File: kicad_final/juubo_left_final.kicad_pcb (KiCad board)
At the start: 2 copper layers, 145.5 x 125.5 mm, 50 parts

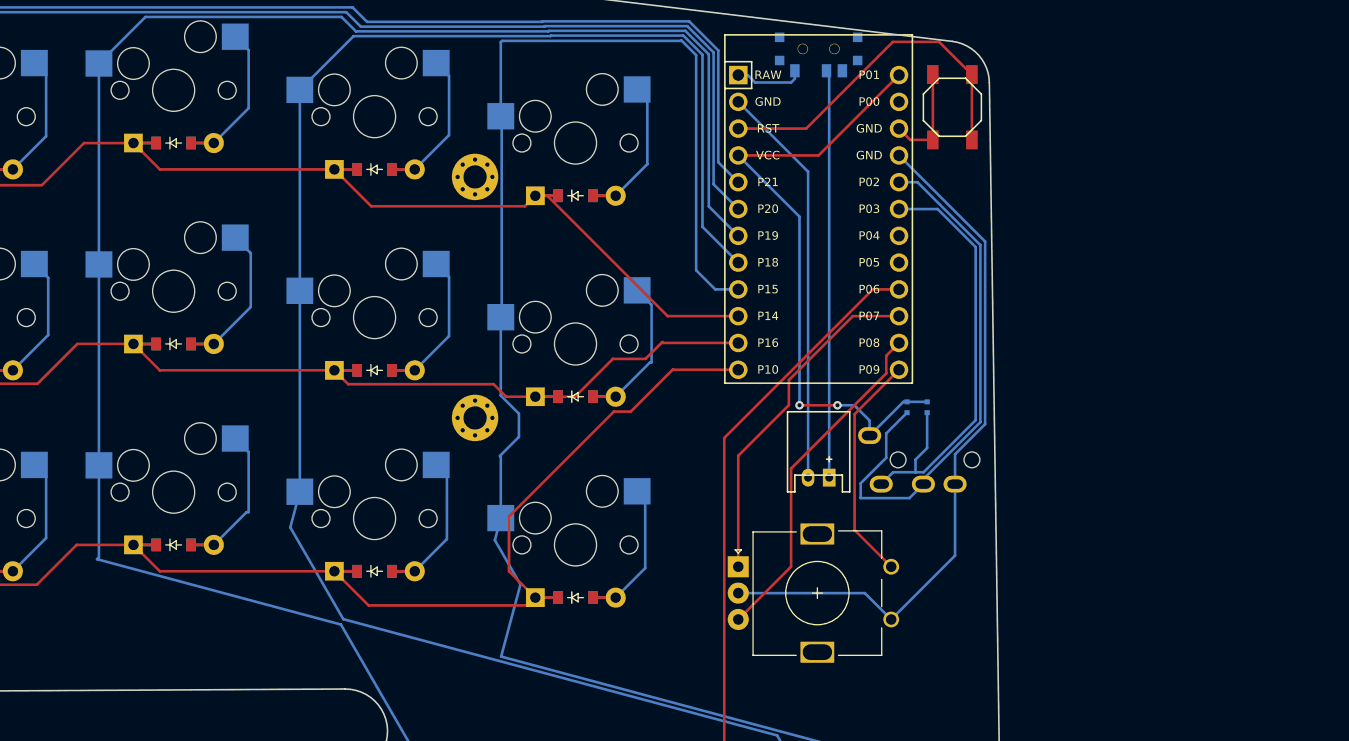
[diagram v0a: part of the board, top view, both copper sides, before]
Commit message: Add qmk, gerber, kicad files
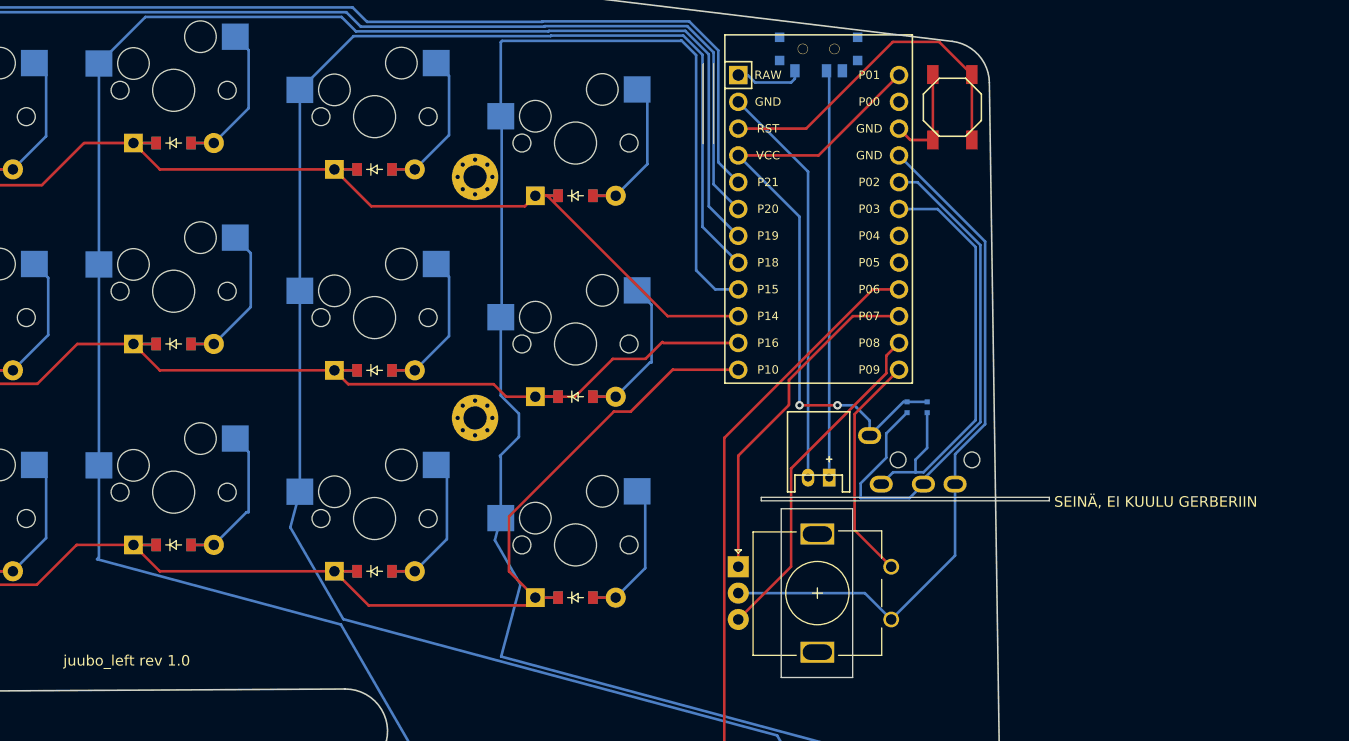
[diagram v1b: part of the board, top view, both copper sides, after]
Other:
- outline, holes or cut-outs redrawn
- board text added: "ROTARY NUPPI 16MM"
- board text added: "SEINÄ, EI KUULU GERBERIIN"
- board text added: "juubo_left rev 1.0"
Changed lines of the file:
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@@
       (outputformat 1)
       (mirror false)
-      (drillshape 1)
+      (drillshape 0)
       (scaleselection 1)
-      (outputdirectory "")
+      (outputdirectory "../gerbers/juube_lefti_final")
     )
   )
@@
       (net 36 "P2") (solder_mask_margin 0.102))
   )
+  (gr_line (start 177.67 57.4) (end 177.67 49.8)
+    (stroke (width 0.05) (type default)) (layer "Edge.Cuts"))
   (gr_arc (start 142.722221 109.098913) (mid 145.877217 110.612025) (end 146.634761 114.028112)
     (stroke (width 0.15) (type solid)) (layer "Edge.Cuts"))
+  (gr_rect (start 182.175 90.925) (end 209.485 91.255)
+    (stroke (width 0.05) (type default)) (fill none) (layer "Edge.Cuts"))
   (gr_arc (start 95.717823 43.355782) (mid 95.889609 43.314727) (end 96.063039 43.281294)
     (stroke (width 0.15) (type solid)) (layer "Edge.Cuts"))
@@
   (gr_arc (start 200.280578 47.697143) (mid 202.774498 48.99265) (end 203.800645 51.608921)
     (stroke (width 0.15) (type solid)) (layer "Edge.Cuts"))
+  (gr_line (start 176.67 57.4) (end 176.67 49.8)
+    (stroke (width 0.05) (type default)) (layer "Edge.Cuts"))
   (gr_line (start 202.748997 162.877717) (end 221.659673 144.499586)
     (stroke (width 0.15) (type default)) (layer "Edge.Cuts"))
@@
   (gr_line (start 143.900962 125.473809) (end 146.634761 114.028112)
     (stroke (width 0.15) (type solid)) (layer "Edge.Cuts"))
+  (gr_rect (start 184.065 92.006) (end 190.84 108.006)
+    (stroke (width 0.05) (type default)) (fill none) (layer "Edge.Cuts"))
   (gr_arc (start 202.748997 162.877717) (mid 200.311135 164.046527) (end 197.688861 163.388522)
     (stroke (width 0.15) (type default)) (layer "Edge.Cuts"))
   (gr_arc (start 221.356714 139.908256) (mid 222.292209 142.152188) (end 221.659673 144.499586)
     (stroke (width 0.15) (type default)) (layer "Edge.Cuts"))
+  (gr_text "juubo_left rev 1.0" (at 116 107) (layer "F.SilkS")
+    (effects (font (size 1 1) (thickness 0.1)) (justify left bottom))
+  )
+  (gr_text "SEINÄ, EI KUULU GERBERIIN" (at 209.94 91.94) (layer "F.SilkS")
+    (effects (font (size 1 1) (thickness 0.15)) (justify left bottom))
+  )
+  (gr_text "ROTARY NUPPI 16MM\n" (at 190.84 100.006) (layer "Edge.Cuts")
+    (effects (font (size 1 1) (thickness 0.15)) (justify left bottom))
+  )
   (segment (start 191.023785 94.035912) (end 191.023785 83.040911) (width 0.25) (layer "F.Cu") (net 1))
   (segment (start 194.493785 97.505912) (end 191.023785 94.035912) (width 0.25) (layer "F.Cu") (net 1))
